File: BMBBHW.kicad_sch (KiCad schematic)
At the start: 15 parts, among them J1 USB_OTG, U1 MDBT50Q-1MV2, U2 AP2112K-3.3, Y1 32.768

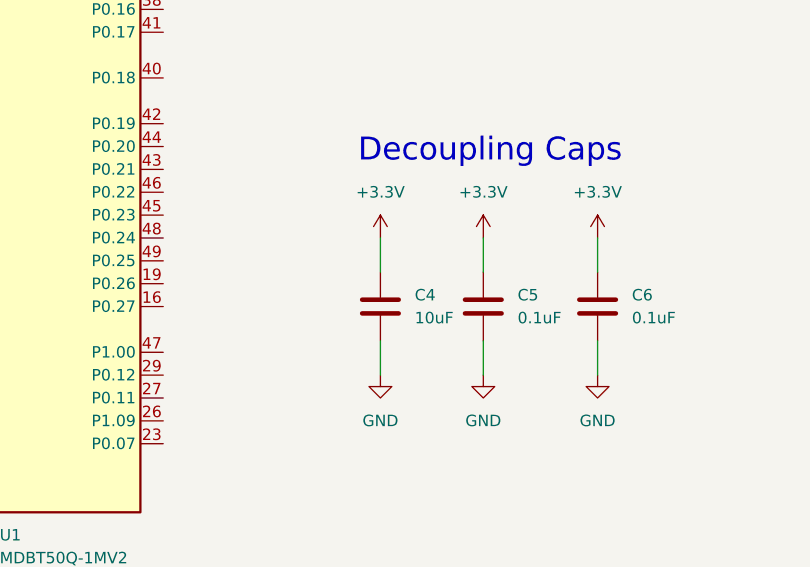
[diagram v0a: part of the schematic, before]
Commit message: Schematic updates
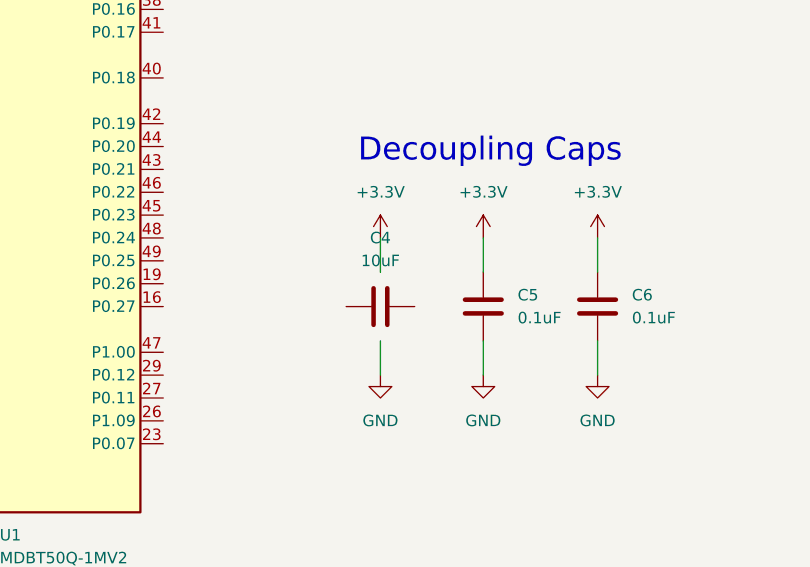
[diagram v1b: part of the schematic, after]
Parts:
- C1, C5, C6: footprint Capacitor_SMD:C_0201_0603Metric -> Capacitor_SMD:C_0603_1608Metric
- C2, R1, R2, R3: footprint (none) -> Capacitor_SMD:C_0603_1608Metric
- C3: footprint (none) -> Capacitor_SMD:C_0805_2012Metric
- C4: footprint Capacitor_SMD:C_0201_0603Metric -> Capacitor_SMD:C_0805_2012Metric
- Y1: footprint Crystal:Crystal_SMD_MicroCrystal_CC7V-T1A-2Pin_3.2x1.5mm -> Crystal:Crystal_SMD_3215-2Pin_3.2x1.5mm
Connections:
- net +3.3V: no longer C4.1
- net GND: no longer C4.2
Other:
- moved on the sheet: C4
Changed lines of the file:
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@@
 			)
 		)
-		(property "Footprint" ""
+		(property "Footprint" "Capacitor_SMD:C_0603_1608Metric"
 			(at 144.78 165.862 90)
 			(effects
@@
 	(symbol
 		(lib_id "Device:C")
-		(at 113.03 93.98 0)
+		(at 113.03 93.98 90)
 		(unit 1)
 		(exclude_from_sim no)
@@
 		(fields_autoplaced yes)
 		(property "Reference" "C4"
-			(at 116.84 92.7099 0)
-			(effects
-				(font
-					(size 1.27 1.27)
-				)
-				(justify left)
+			(at 113.03 86.36 90)
+			(effects
+				(font
+					(size 1.27 1.27)
+				)
 			)
 		)
 		(property "Value" "10uF"
-			(at 116.84 95.2499 0)
-			(effects
-				(font
-					(size 1.27 1.27)
-				)
-				(justify left)
-			)
-		)
-		(property "Footprint" "Capacitor_SMD:C_0201_0603Metric"
-			(at 113.9952 97.79 0)
+			(at 113.03 88.9 90)
+			(effects
+				(font
+					(size 1.27 1.27)
+				)
+			)
+		)
+		(property "Footprint" "Capacitor_SMD:C_0805_2012Metric"
+			(at 116.84 93.0148 0)
 			(effects
 				(font
@@
 			)
 		)
-		(property "Footprint" ""
+		(property "Footprint" "Capacitor_SMD:C_0805_2012Metric"
 			(at 60.6552 175.26 0)
 			(effects
@@
 			)
 		)
-		(property "Footprint" "Crystal:Crystal_SMD_MicroCrystal_CC7V-T1A-2Pin_3.2x1.5mm"
+		(property "Footprint" "Crystal:Crystal_SMD_3215-2Pin_3.2x1.5mm"
 			(at 109.22 39.37 0)
 			(effects
@@
 			)
 		)
-		(property "Footprint" ""
+		(property "Footprint" "Capacitor_SMD:C_0603_1608Metric"
 			(at 70.612 171.45 90)
 			(effects
@@
 			)
 		)
-		(property "Footprint" "Capacitor_SMD:C_0201_0603Metric"
+		(property "Footprint" "Capacitor_SMD:C_0603_1608Metric"
 			(at 119.38 33.9852 0)
 			(effects
@@
 			)
 		)
-		(property "Footprint" ""
+		(property "Footprint" "Capacitor_SMD:C_0603_1608Metric"
 			(at 119.38 46.6852 0)
 			(effects
@@
 			)
 		)
-		(property "Footprint" ""
+		(property "Footprint" "Capacitor_SMD:C_0603_1608Metric"
 			(at 144.78 168.402 90)
 			(effects
@@
 			)
 		)
-		(property "Footprint" "Capacitor_SMD:C_0201_0603Metric"
+		(property "Footprint" "Capacitor_SMD:C_0603_1608Metric"
 			(at 138.1252 97.79 0)
 			(effects
@@
 			)
 		)
-		(property "Footprint" "Capacitor_SMD:C_0201_0603Metric"
+		(property "Footprint" "Capacitor_SMD:C_0603_1608Metric"
 			(at 125.4252 97.79 0)
 			(effects
